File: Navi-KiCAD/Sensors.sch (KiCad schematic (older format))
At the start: 12 parts, among them U11 MPU-9250, U12 LPS25HBTR

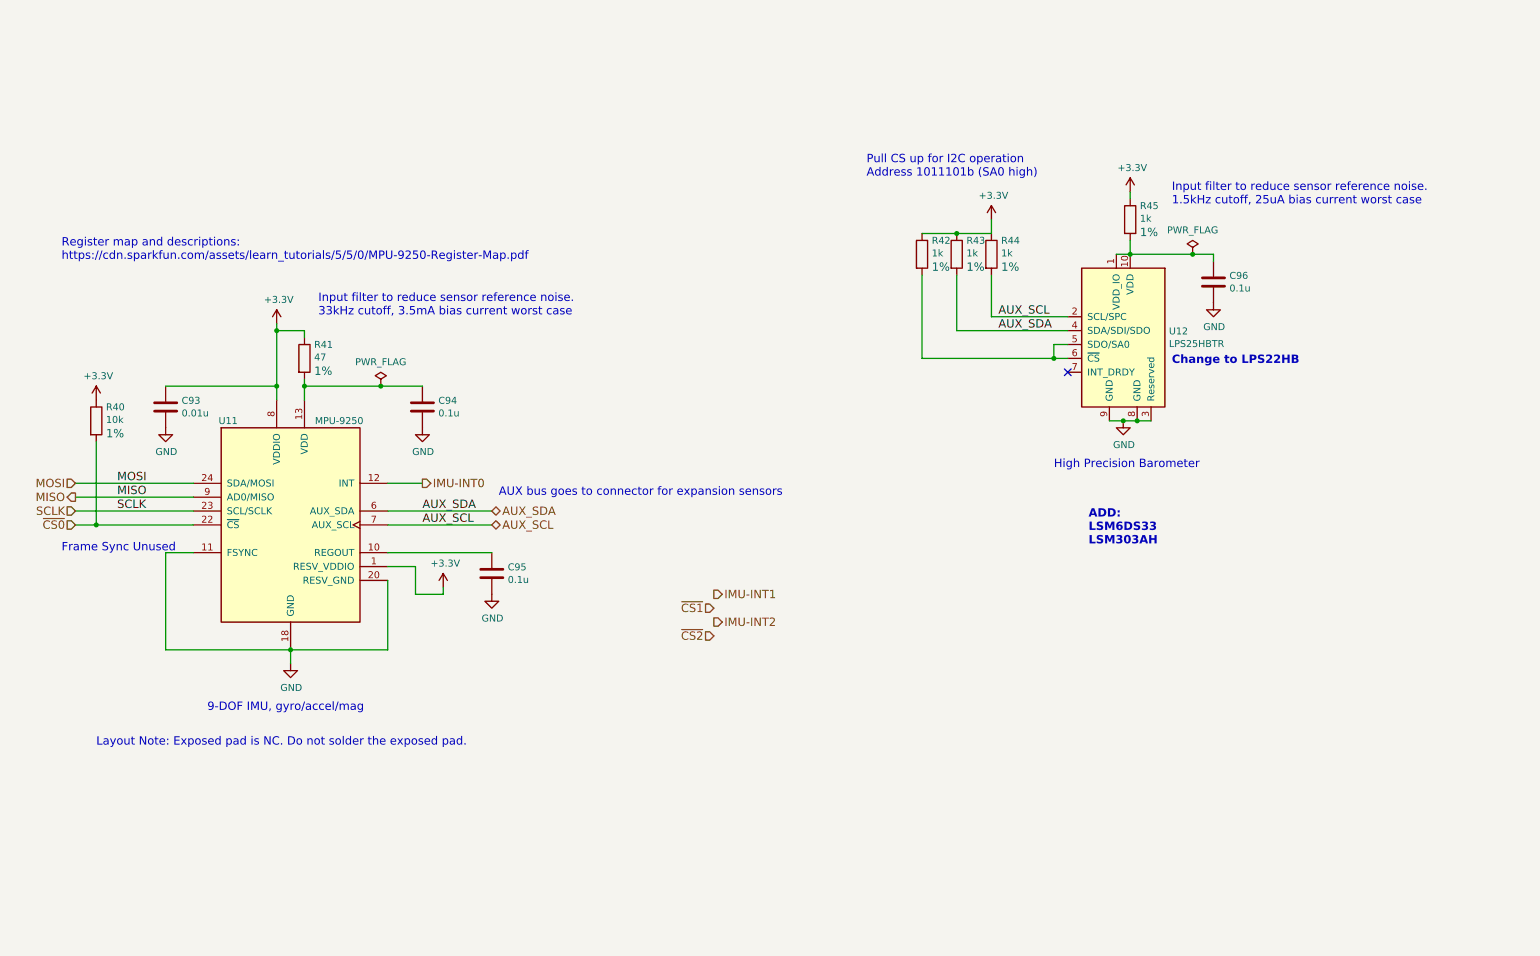
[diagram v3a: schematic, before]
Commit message: Added additional sensors
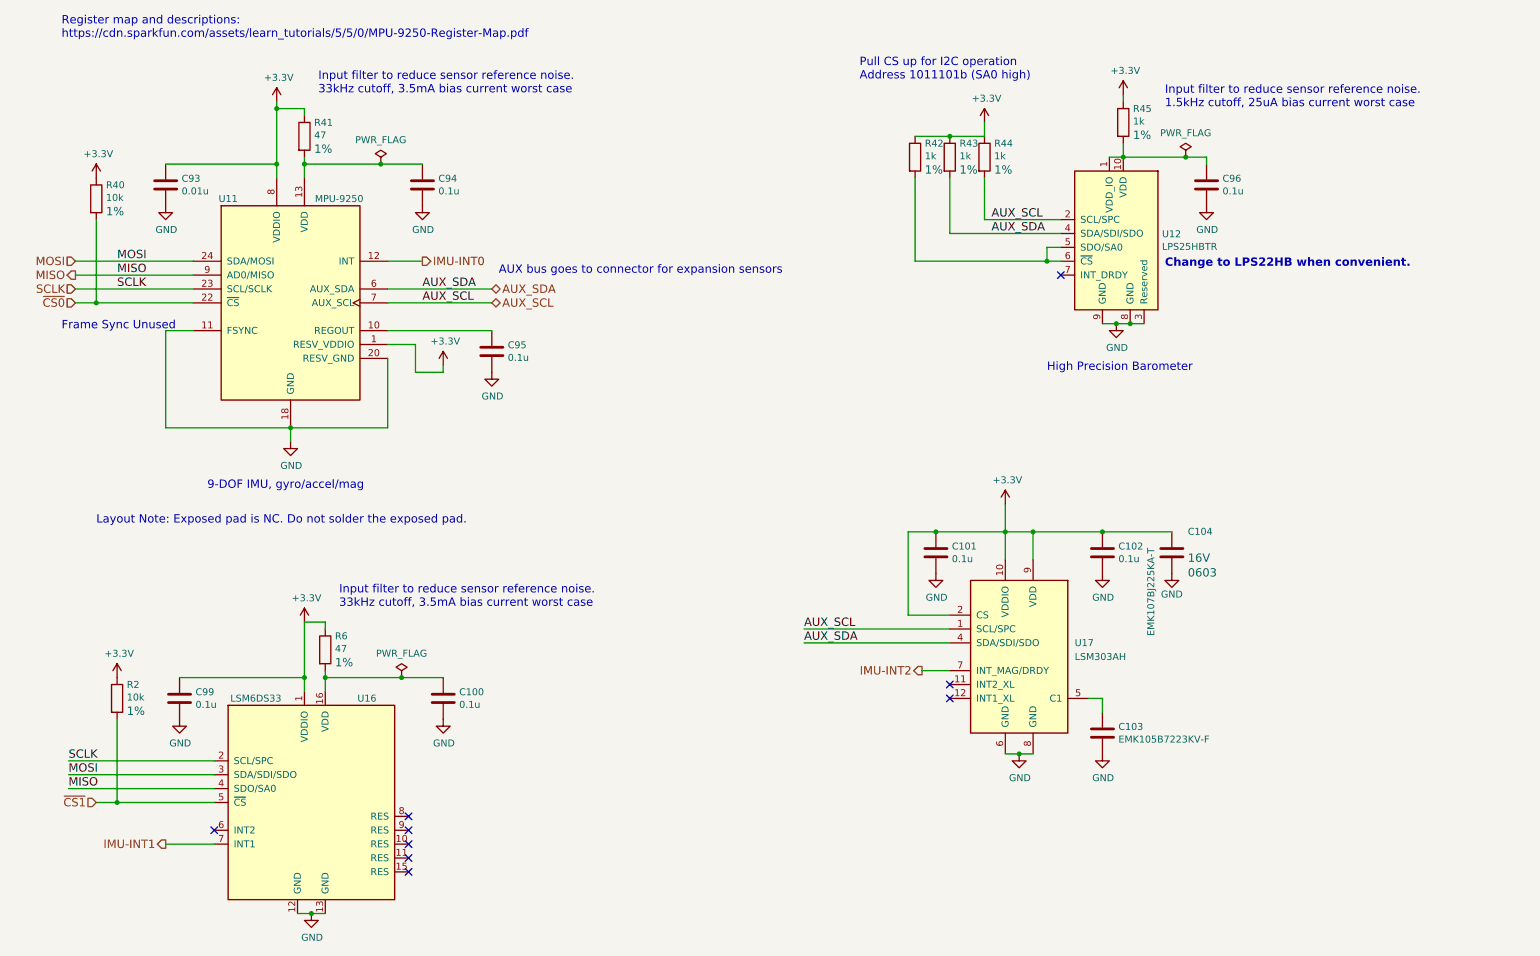
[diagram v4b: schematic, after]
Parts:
- added C100, C101, C102, C99: 0.1u, Capacitors_SMD:C_0402, symbol C
- added C103: EMK105B7223KV-F, Capacitors_SMD:C_0402, symbol C
- added C104: EMK107BJ225KA-T, Capacitors_SMD:C_0603, symbol C
- added R2: 10k, Resistors_SMD:R_0402, symbol R
- added R6: 47, Resistors_SMD:R_0402, symbol R
- added U16: LSM6DS33, Housings_LGA:LGA-16L_3x3mm_Pitch0.5mm, symbol LSM6DS33
- added U17: LSM303AH, Housings_LGA:LGA-12_2x2mm_Pitch0.5mm, symbol LSM303AH
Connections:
- net +3V3: now also C101.1, C102.1, C104.1, C99.1, R2.1, R6.1, U16.1 (VDDIO), U17.10 (VDDIO), U17.2 (CS), U17.9 (VDD)
- net AUX_SCL: now also U17.1 (SCL/SPC)
- net AUX_SDA: now also U17.4 (SDA/SDI/SDO)
- net GND: now also C100.2, C101.2, C102.2, C103.2, C104.2, C99.2, U16.12 (GND), U16.13 (GND), U17.6 (GND), U17.8 (GND)
- net IMU-INT1: now also U16.7 (INT1)
- net IMU-INT2: now also U17.7 (INT_MAG/DRDY)
- net MISO: now also U16.4 (SDO/SA0)
- net MOSI: now also U16.3 (SDA/SDI/SDO)
- net SCLK: now also U16.2 (SCL/SPC)
- net ~CS1: now also R2.2, U16.5 (~CS)
- new net: C100.1, R6.2, U16.16 (VDD)
- new net: C103.1, U17.5 (C1)
- no-connect marks 1 -> 9
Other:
- note added: "Change to LPS22HB when convenient."
- note removed: "ADD:\nLSM6DS33\nLSM303AH"
- note removed: "Change to LPS22HB"
- moved on the sheet: C93, C94, C95, C96, R40, R41, R42, R43, R44, R45, U11, U12

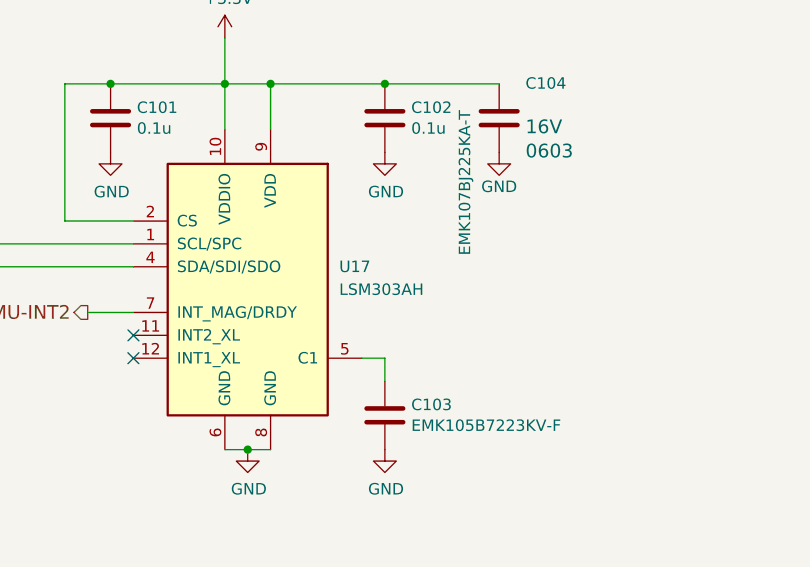
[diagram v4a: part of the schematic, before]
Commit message: Tweaked pinouts and finished routing known connectors. Now for the remaining IO.
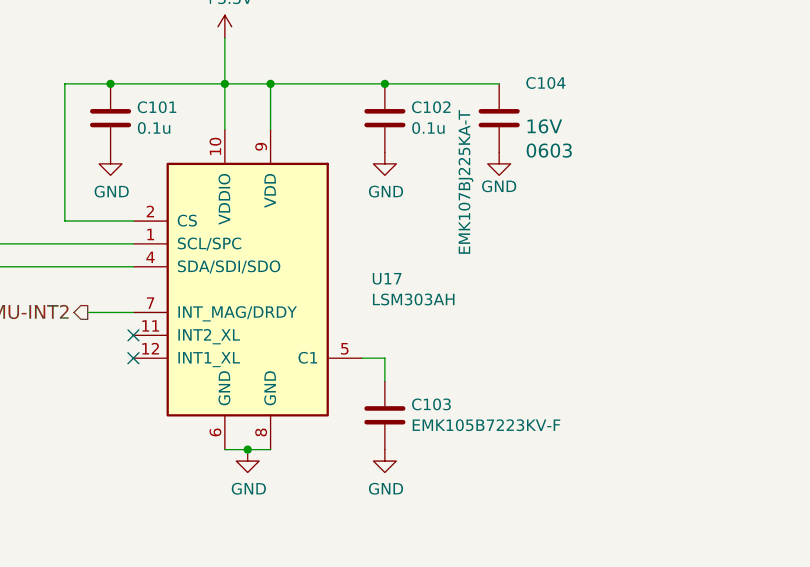
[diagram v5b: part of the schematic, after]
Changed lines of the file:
@@
 $EndComp
 $Comp
-L GND #PWR100
+L GND #PWR0107
 U 1 1 58B4AF5E
 P 2400 3700
-F 0 "#PWR100" H -1950 -100 50  0001 C CNN
+F 0 "#PWR0107" H -1950 -100 50  0001 C CNN
 F 1 "GND" H 2405 3527 50  0000 C CNN
 F 2 "" H -1950 150 50  0001 C CNN
@@
 $EndComp
 $Comp
-L +3.3V #PWR99
+L +3.3V #PWR0108
 U 1 1 58B4AFA2
 P 2300 1250
-F 0 "#PWR99" H -2200 -2300 50  0001 C CNN
+F 0 "#PWR0108" H -2200 -2300 50  0001 C CNN
 F 1 "+3.3V" H 2315 1423 50  0000 C CNN
 F 2 "" H -2200 -2150 50  0001 C CNN
@@
 $EndComp
 $Comp
-L GND #PWR113
+L GND #PWR0109
 U 1 1 58B4B105
 P 8350 2850
-F 0 "#PWR113" H 4000 -950 50  0001 C CNN
+F 0 "#PWR0109" H 4000 -950 50  0001 C CNN
 F 1 "GND" H 8355 2677 50  0000 C CNN
 F 2 "" H 4000 -700 50  0001 C CNN
@@
 Connection ~ 8350 2850
 $Comp
-L +3.3V #PWR114
+L +3.3V #PWR0110
 U 1 1 58B4B14B
 P 8400 1200
-F 0 "#PWR114" H 3900 -2350 50  0001 C CNN
+F 0 "#PWR0110" H 3900 -2350 50  0001 C CNN
 F 1 "+3.3V" H 8415 1373 50  0000 C CNN
 F 2 "" H 3900 -2200 50  0001 C CNN
@@
 Connection ~ 8400 1650
 $Comp
-L GND #PWR116
+L GND #PWR0111
 U 1 1 58B4B9E9
 P 9000 2000
-F 0 "#PWR116" H 4650 -1800 50  0001 C CNN
+F 0 "#PWR0111" H 4650 -1800 50  0001 C CNN
 F 1 "GND" H 9005 1827 50  0000 C CNN
 F 2 "" H 4650 -1550 50  0001 C CNN
@@
 Input filter to reduce sensor reference noise. \n1.5kHz cutoff, 25uA bias current worst case
 $Comp
-L +3.3V #PWR108
+L +3.3V #PWR0112
 U 1 1 58B4C158
 P 7400 1400
-F 0 "#PWR108" H 2900 -2150 50  0001 C CNN
+F 0 "#PWR0112" H 2900 -2150 50  0001 C CNN
 F 1 "+3.3V" H 7415 1573 50  0000 C CNN
 F 2 "" H 2900 -2000 50  0001 C CNN
@@
 	3100 2900 3850 2900
 $Comp
-L GND #PWR106
+L GND #PWR0113
 U 1 1 58B4FB3E
 P 3850 3200
-F 0 "#PWR106" H -500 -600 50  0001 C CNN
+F 0 "#PWR0113" H -500 -600 50  0001 C CNN
 F 1 "GND" H 3855 3027 50  0000 C CNN
 F 2 "" H -500 -350 50  0001 C CNN
@@
 	3500 3200 3500 3150
 $Comp
-L +3.3V #PWR104
+L +3.3V #PWR0114
 U 1 1 58B50137
 P 3500 3150
-F 0 "#PWR104" H -1000 -400 50  0001 C CNN
+F 0 "#PWR0114" H -1000 -400 50  0001 C CNN
 F 1 "+3.3V" H 3515 3323 50  0000 C CNN
 F 2 "" H -1000 -250 50  0001 C CNN
@@
 IMU-INT0
 $Comp
-L GND #PWR103
+L GND #PWR0115
 U 1 1 58B505FC
 P 3350 2000
-F 0 "#PWR103" H -1000 -1800 50  0001 C CNN
+F 0 "#PWR0115" H -1000 -1800 50  0001 C CNN
 F 1 "GND" H 3355 1827 50  0000 C CNN
 F 2 "" H -1000 -1550 50  0001 C CNN
@@
 Input filter to reduce sensor reference noise. \n33kHz cutoff, 3.5mA bias current worst case
 $Comp
-L GND #PWR97
+L GND #PWR0116
 U 1 1 58B50B96
 P 1500 2000
-F 0 "#PWR97" H -2850 -1800 50  0001 C CNN
+F 0 "#PWR0116" H -2850 -1800 50  0001 C CNN
 F 1 "GND" H 1505 1827 50  0000 C CNN
 F 2 "" H -2850 -1550 50  0001 C CNN
@@
 NoConn ~ 7950 2500
 $Comp
-L PWR_FLAG #FLG13
+L PWR_FLAG #FLG0117
 U 1 1 58BF1DC3
 P 3050 1700
-F 0 "#FLG13" H -1800 -1475 50  0001 C CNN
+F 0 "#FLG0117" H -1800 -1475 50  0001 C CNN
 F 1 "PWR_FLAG" H 3050 1874 50  0000 C CNN
 F 2 "" H -1800 -1550 50  0001 C CNN
@@
 Connection ~ 3050 1700
 $Comp
-L PWR_FLAG #FLG15
+L PWR_FLAG #FLG0118
 U 1 1 58BF1E5B
 P 8850 1650
-F 0 "#FLG15" H 4000 -1525 50  0001 C CNN
+F 0 "#FLG0118" H 4000 -1525 50  0001 C CNN
 F 1 "PWR_FLAG" H 8850 1824 50  0000 C CNN
 F 2 "" H 4000 -1600 50  0001 C CNN
@@
 $EndComp
 $Comp
-L +3.3V #PWR95
+L +3.3V #PWR0119
 U 1 1 58D7F763
 P 1000 1800
-F 0 "#PWR95" H -3500 -1750 50  0001 C CNN
+F 0 "#PWR0119" H -3500 -1750 50  0001 C CNN
 F 1 "+3.3V" H 1015 1973 50  0000 C CNN
 F 2 "" H -3500 -1600 50  0001 C CNN
@@
 $EndComp
 $Comp
-L LSM303AH U17
-U 1 1 58F65BC1
-P 7650 5250
-F 0 "U17" H 8050 5350 50  0000 L CNN
-F 1 "LSM303AH" H 8050 5250 50  0000 L CNN
-F 2 "Housings_LGA:LGA-12_2x2mm_Pitch0.5mm" H -1400 -550 50  0001 L CNN
-F 3 "http://www.st.com/content/ccc/resource/technical/document/datasheet/1b/a1/fd/09/9f/41/44/cf/DM00177690.pdf/files/DM00177690.pdf/jcr:content/translations/en.DM00177690.pdf" H -1500 800 50  0001 C CNN
-	1    7650 5250
-	1    0    0    -1
-$EndComp
-$Comp
 L R R6
 U 1 1 58F66310
@@
 Input filter to reduce sensor reference noise. \n33kHz cutoff, 3.5mA bias current worst case
 $Comp
-L PWR_FLAG #FLG14
+L PWR_FLAG #FLG0120
 U 1 1 58F66326
 P 3200 5400
-F 0 "#FLG14" H -1650 2225 50  0001 C CNN
+F 0 "#FLG0120" H -1650 2225 50  0001 C CNN
 F 1 "PWR_FLAG" H 3200 5574 50  0000 C CNN
 F 2 "" H -1650 2150 50  0001 C CNN
@@
 Connection ~ 3200 5400
 $Comp
-L GND #PWR105
+L GND #PWR0121
 U 1 1 58F66C6D
 P 3500 5700
-F 0 "#PWR105" H -850 1900 50  0001 C CNN
+F 0 "#PWR0121" H -850 1900 50  0001 C CNN
 F 1 "GND" H 3505 5527 50  0000 C CNN
 F 2 "" H -850 2150 50  0001 C CNN
@@
 $EndComp
 $Comp
-L +3.3V #PWR101
+L +3.3V #PWR0122
 U 1 1 58F66DF8
 P 2500 5000
-F 0 "#PWR101" H -2000 1450 50  0001 C CNN
+F 0 "#PWR0122" H -2000 1450 50  0001 C CNN
 F 1 "+3.3V" H 2515 5173 50  0000 C CNN
 F 2 "" H -2000 1600 50  0001 C CNN
@@
 $EndComp
 $Comp
-L GND #PWR98
+L GND #PWR0123
 U 1 1 58F6775E
 P 1600 5700
-F 0 "#PWR98" H -2750 1900 50  0001 C CNN
+F 0 "#PWR0123" H -2750 1900 50  0001 C CNN
 F 1 "GND" H 1605 5527 50  0000 C CNN
 F 2 "" H -2750 2150 50  0001 C CNN
@@
 $EndComp
 $Comp
-L +3.3V #PWR96
+L +3.3V #PWR0124
 U 1 1 58F67D7B
 P 1150 5400
-F 0 "#PWR96" H -3350 1850 50  0001 C CNN
+F 0 "#PWR0124" H -3350 1850 50  0001 C CNN
 F 1 "+3.3V" H 1165 5573 50  0000 C CNN
 F 2 "" H -3350 2000 50  0001 C CNN
@@
 	7150 5350 6950 5350
 $Comp
-L GND #PWR102
+L GND #PWR0125
 U 1 1 58F68607
 P 2550 7100
-F 0 "#PWR102" H -1800 3300 50  0001 C CNN
+F 0 "#PWR0125" H -1800 3300 50  0001 C CNN
 F 1 "GND" H 2555 6927 50  0000 C CNN
 F 2 "" H -1800 3550 50  0001 C CNN
@@
 Connection ~ 2550 7100
 $Comp
-L GND #PWR110
+L GND #PWR0126
 U 1 1 58F68874
 P 7650 5950
-F 0 "#PWR110" H 3300 2150 50  0001 C CNN
+F 0 "#PWR0126" H 3300 2150 50  0001 C CNN
 F 1 "GND" H 7655 5777 50  0000 C CNN
 F 2 "" H 3300 2400 50  0001 C CNN
@@
 	6100 5050 7150 5050
 $Comp
-L +3.3V #PWR109
+L +3.3V #PWR0127
 U 1 1 58F6A64F
 P 7550 4150
-F 0 "#PWR109" H 3050 600 50  0001 C CNN
+F 0 "#PWR0127" H 3050 600 50  0001 C CNN
 F 1 "+3.3V" H 7565 4323 50  0000 C CNN
 F 2 "" H 3050 750 50  0001 C CNN
@@
 	8250 5550 8250 5650
 $Comp
-L GND #PWR112
+L GND #PWR0128
 U 1 1 58F6ACC0
 P 8250 5950
-F 0 "#PWR112" H 3900 2150 50  0001 C CNN
+F 0 "#PWR0128" H 3900 2150 50  0001 C CNN
 F 1 "GND" H 8255 5777 50  0000 C CNN
 F 2 "" H 3900 2400 50  0001 C CNN
@@
 $EndComp
 $Comp
-L GND #PWR111
+L GND #PWR0129
 U 1 1 58F6D6EF
 P 8250 4650
-F 0 "#PWR111" H 3900 850 50  0001 C CNN
+F 0 "#PWR0129" H 3900 850 50  0001 C CNN
 F 1 "GND" H 8255 4477 50  0000 C CNN
 F 2 "" H 3900 1100 50  0001 C CNN
@@
 $EndComp
 $Comp
-L GND #PWR115
+L GND #PWR0130
 U 1 1 58F80A2F
 P 8750 4650
-F 0 "#PWR115" H 8750 4400 50  0001 C CNN
+F 0 "#PWR0130" H 8750 4400 50  0001 C CNN
 F 1 "GND" H 8750 4500 50  0000 C CNN
 F 2 "" H 8750 4650 50  0001 C CNN
@@
 $EndComp
 $Comp
-L GND #PWR107
+L GND #PWR0131
 U 1 1 58F80F79
 P 7050 4650
-F 0 "#PWR107" H 2700 850 50  0001 C CNN
+F 0 "#PWR0131" H 2700 850 50  0001 C CNN
 F 1 "GND" H 7055 4477 50  0000 C CNN
 F 2 "" H 2700 1100 50  0001 C CNN
@@
 	6850 4950 6850 4350
 Connection ~ 7050 4350
+$Comp
+L LSM303AH U17
+U 1 1 58FC3C43
+P 7650 5250
+F 0 "U17" H 8191 5296 50  0000 L CNN
+F 1 "LSM303AH" H 8191 5205 50  0000 L CNN
+F 2 "Housings_LGA:LGA-12_2x2mm_Pitch0.5mm" H 50  -450 50  0001 L CNN
+F 3 "www.st.com/resource/en/datasheet/lsm303ah.pdf" H -50 900 50  0001 C CNN
+	1    7650 5250
+	1    0    0    -1
+$EndComp
 $EndSCHEMATC

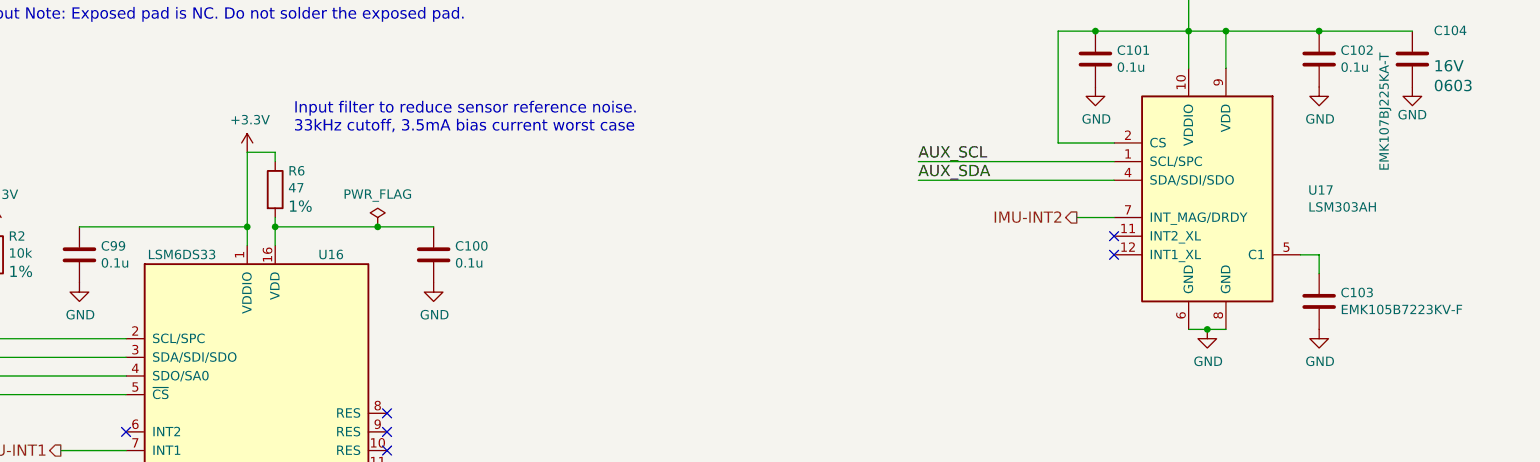
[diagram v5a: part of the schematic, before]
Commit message: Cleaned up silkscreen.
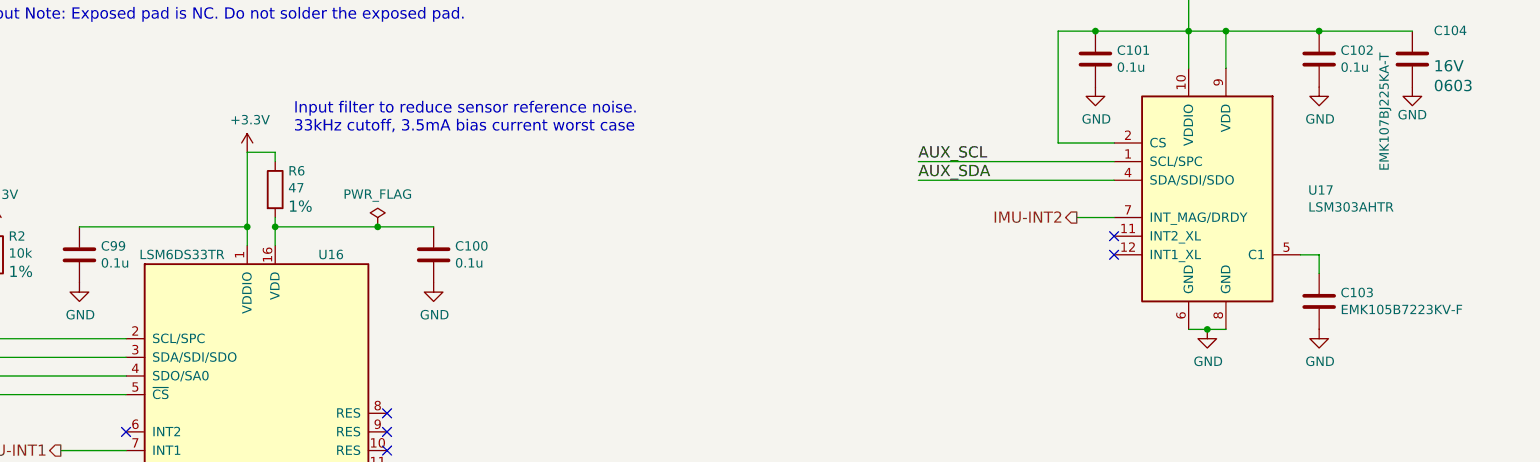
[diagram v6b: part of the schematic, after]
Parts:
- U16: value LSM6DS33 -> LSM6DS33TR
- U17: value LSM303AH -> LSM303AHTR
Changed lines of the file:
@@
 P 2550 6300
 F 0 "U16" H 2950 7050 50  0000 C CNN
-F 1 "LSM6DS33" H 2150 7050 50  0000 C CNN
+F 1 "LSM6DS33TR" H 2150 7050 50  0000 C CNN
 F 2 "Housings_LGA:LGA-16L_3x3mm_Pitch0.5mm" H -3100 2250 50  0001 C CNN
 F 3 "http://www.st.com/content/ccc/resource/technical/document/datasheet/ed/aa/b8/e5/ab/3a/41/df/DM00157718.pdf/files/DM00157718.pdf/jcr:content/translations/en.DM00157718.pdf" H -4600 2650 50  0001 C CNN
@@
 P 7650 5250
 F 0 "U17" H 8191 5296 50  0000 L CNN
-F 1 "LSM303AH" H 8191 5205 50  0000 L CNN
+F 1 "LSM303AHTR" H 8191 5205 50  0000 L CNN
 F 2 "Housings_LGA:LGA-12_2x2mm_Pitch0.5mm" H 50  -450 50  0001 L CNN
 F 3 "www.st.com/resource/en/datasheet/lsm303ah.pdf" H -50 900 50  0001 C CNN
